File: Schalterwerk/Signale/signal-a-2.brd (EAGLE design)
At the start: 100.3 x 80 mm, 50 parts, among them Q1 NPN-23, Q2 NPN-23, Q3 NPN-23, Q4 NPN-23, X1 PHNX_4P_508CONN_1017493, X2 PHNX_4P_508CONN_1017493, X3 IO-HAT, X4 PHNX_4P_350CONN_1984989_PXC, X5 PHNX_4P_350CONN_1984989_PXC, X6 RJ45-JACK

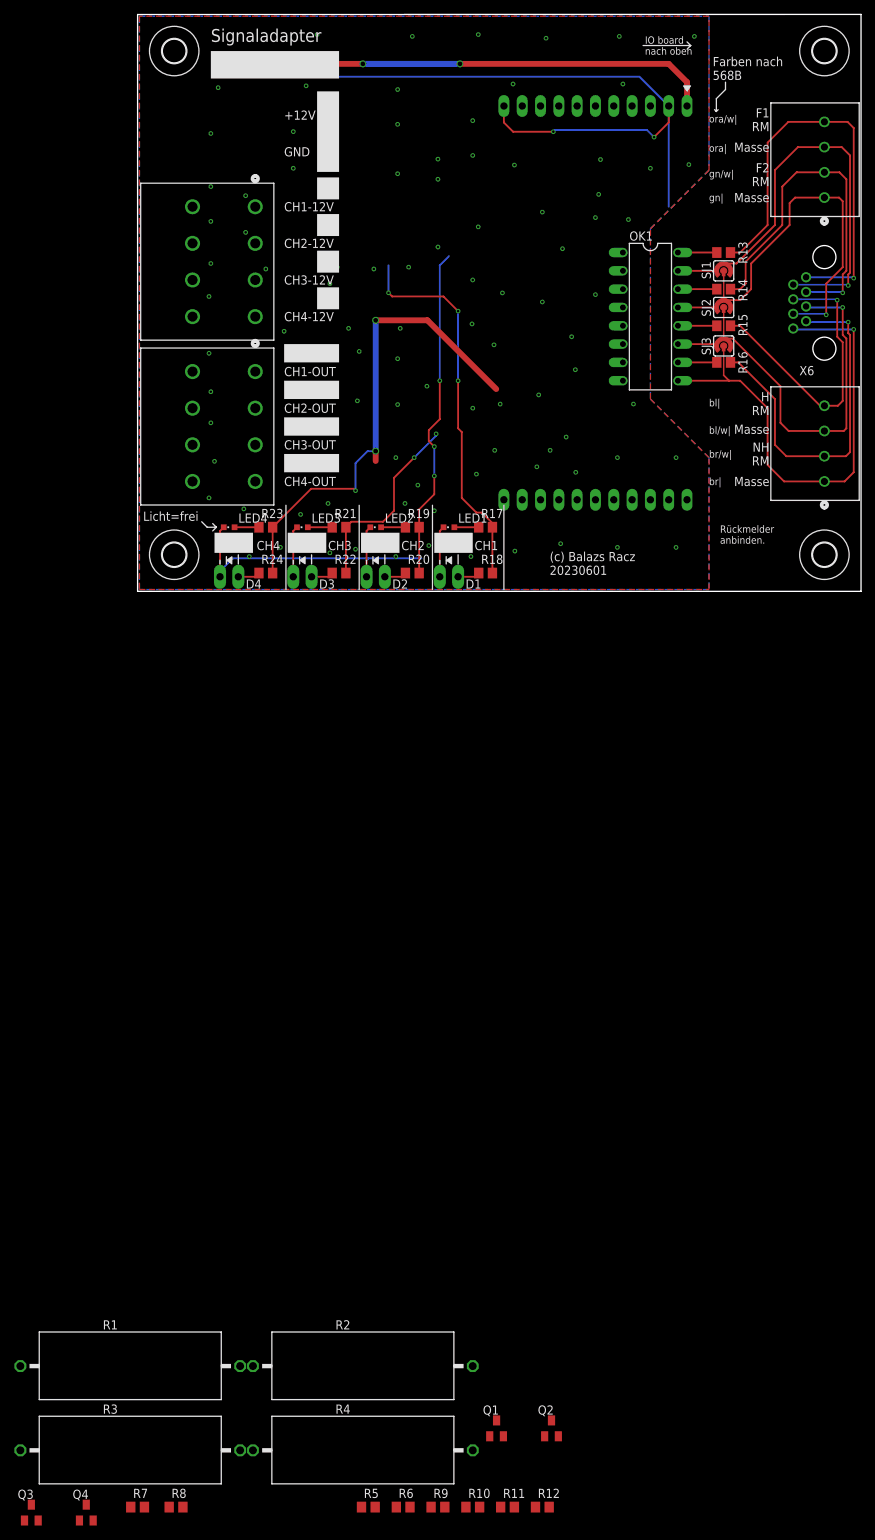
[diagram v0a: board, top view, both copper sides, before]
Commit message: Finishes layout of signal adapter. Adds side connector for IO.
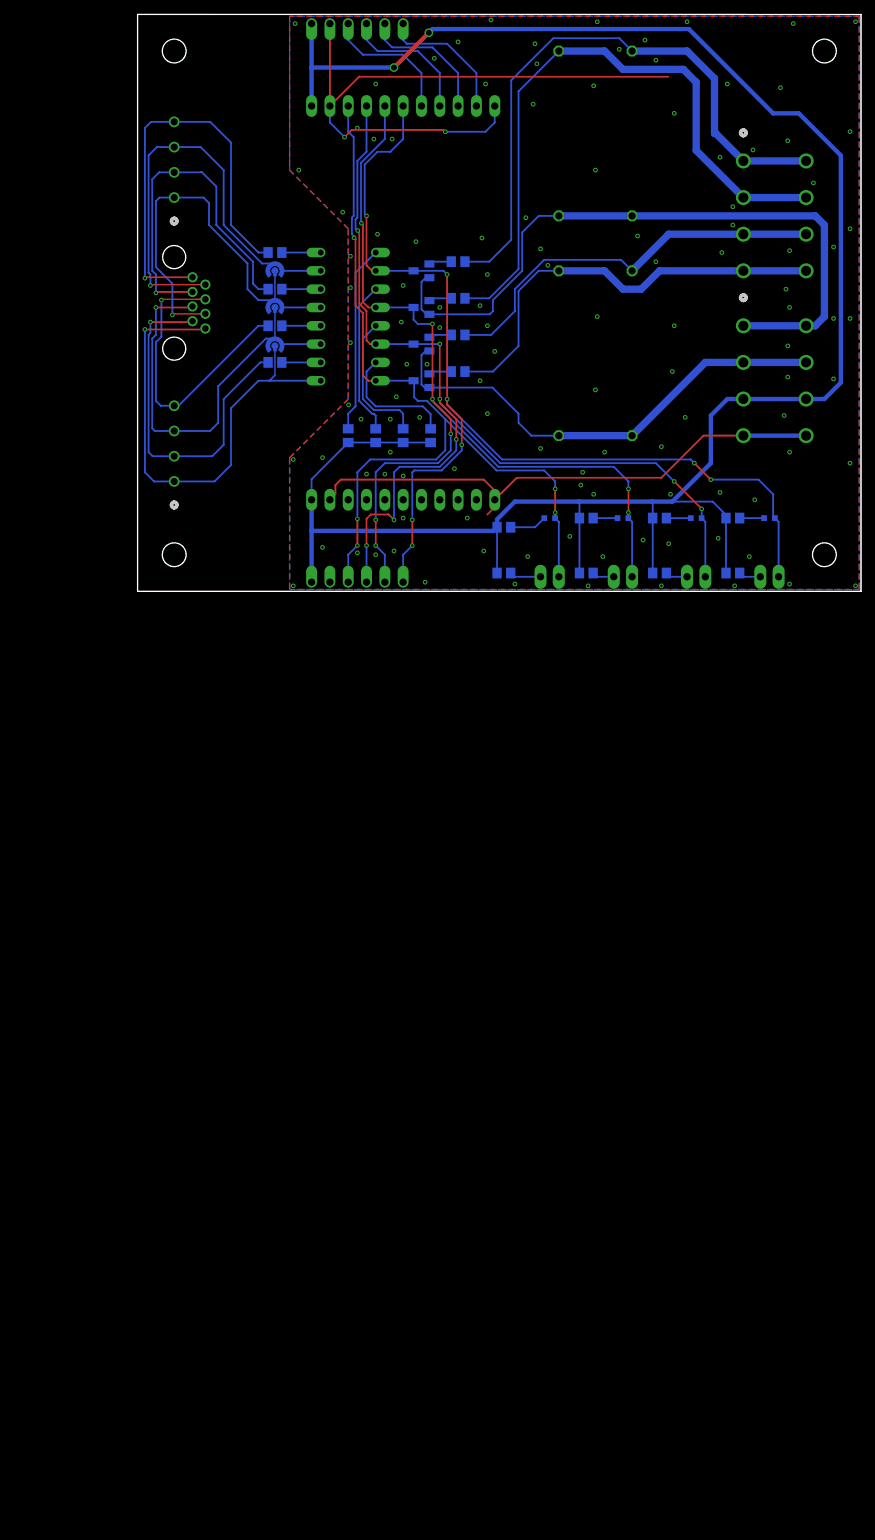
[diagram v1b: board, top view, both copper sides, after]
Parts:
- added JP1, JP2: (no value), eagleparts:1X06
- R1, R2, R3, R4: device rcl:VTA52 -> rcl:0617/22
- moved R1 184.6 mm to (68.6, 63.5), flipped to the bottom, turned to 270 degrees
- moved R5 173.2 mm to (44.5, 45.7), flipped to the bottom, turned to 180 degrees
- moved R2 173.1 mm to (58.4, 63.5), flipped to the bottom, turned to 270 degrees
- moved Q3 170.8 mm to (39.4, 34.3), flipped to the bottom, turned to 270 degrees
- moved R7 168.5 mm to (44.5, 35.6), flipped to the bottom, turned to 180 degrees
- moved R6 167.8 mm to (44.5, 40.6), flipped to the bottom, turned to 180 degrees
- moved R3 167.3 mm to (68.6, 33.0), flipped to the bottom, turned to 270 degrees
- moved Q4 163.7 mm to (39.4, 29.2), flipped to the bottom, turned to 270 degrees
- moved R8 162.3 mm to (44.5, 30.5), flipped to the bottom, turned to 180 degrees
- moved Q1 160.9 mm to (39.4, 44.5), flipped to the bottom, turned to 270 degrees
- moved Q2 156.5 mm to (39.4, 39.4), flipped to the bottom, turned to 270 degrees
- moved R4 154.6 mm to (58.4, 33.0), flipped to the bottom, turned to 270 degrees
- moved R12 149.4 mm to (40.6, 21.6), flipped to the bottom, turned to 270 degrees
- moved R11 149.3 mm to (36.8, 21.6), flipped to the bottom, turned to 270 degrees
- moved R10 149.2 mm to (33.0, 21.6), flipped to the bottom, turned to 270 degrees
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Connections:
- removed net 12V2: X3.P$22
- removed net N$10: R19.2, R20.2
- removed net N$11: R21.2, R22.2
- removed net N$13: R23.2, R24.2
- removed net N$14: D4.C, LED4.C
- removed net N$28: OK1.2, Q1.3
- removed net N$33: OK1.4, Q2.3
- removed net N$38: OK1.6, Q3.3
- removed net N$40: OK1.8, Q4.3
- new net N$2: D1.C, JP2.4, LED1.C, OK1.8, Q4.3, X3.P$3
- new net N$5: D3.C, JP2.3, LED3.C, OK1.6, Q3.3, X3.P$4
- new net N$7: D2.C, JP2.2, LED2.C, OK1.4, Q2.3, X3.P$5
- new net N$9: D4.C, JP2.1, LED4.C, OK1.2, Q1.3, X3.P$6
- net +12V: now also JP1.1, JP2.6, R17.2, R18.2, R19.2, R20.2, R21.2, R22.2, R23.2, R24.2, X3.P$22
- net GND: now also JP1.2, JP2.5
- net N$1: now also JP1.6, X3.P$10; no longer R17.2, R18.2
- net N$3: now also JP1.5, X3.P$9; no longer D1.C, LED1.C
- net N$4: now also JP1.4, X3.P$8; no longer D2.C, LED2.C
- net N$6: now also JP1.3, X3.P$7; no longer D3.C, LED3.C
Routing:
- net +12V: track 57.1 -> 287.6 mm
- net N$9: track 0.00 -> 149.2 mm, vias 0 -> 8
- net N$5: track 0.00 -> 142.1 mm, vias 0 -> 8
- net N$7: track 0.00 -> 132.1 mm, vias 0 -> 8
- net N$2: track 0.00 -> 119.4 mm, vias 0 -> 5
- net RL-F: track 0.00 -> 96.0 mm
- net F2: track 0.00 -> 89.9 mm
- net F1: track 0.00 -> 84.6 mm
- net GND: track 91.9 -> 165.3 mm, vias 105 -> 120
- net N$13: track 67.6 -> 0.00 mm, vias 3 -> 0
- net RL-H: track 0.00 -> 66.6 mm
- net NH: track 0.00 -> 59.7 mm
- net H: track 0.00 -> 56.1 mm
- net N$10: track 46.3 -> 0.00 mm, vias 3 -> 0
- net N$14: track 36.9 -> 0.00 mm
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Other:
- board text added: "(c) Balazs Racz 20230604"
- board text added: "F1"
- board text added: "F2"
- board text added: "H"
- board text added: "NH"
- board text added: "RL-F"
- board text added: "RL-H"
- board text removed: "(c) Balazs Racz 20230601"
- board text removed: "CH1"
- board text removed: "CH1-12V"
- board text removed: "CH1-OUT"
- board text removed: "CH2"
- board text removed: "CH2-12V"
- board text removed: "CH2-OUT"
- board text removed: "CH3"
- board text removed: "CH3-12V"
- board text removed: "CH3-OUT"
- board text removed: "CH4"
- board text removed: "CH4-12V"
- board text removed: "CH4-OUT"
- board text removed: "Licht=frei"
